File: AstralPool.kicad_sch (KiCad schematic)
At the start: 21 parts, among them J1 RJ12, J2 RJ12, J3 Header, Q1 2N3904, U1 LM2678T-5.0/NOPB

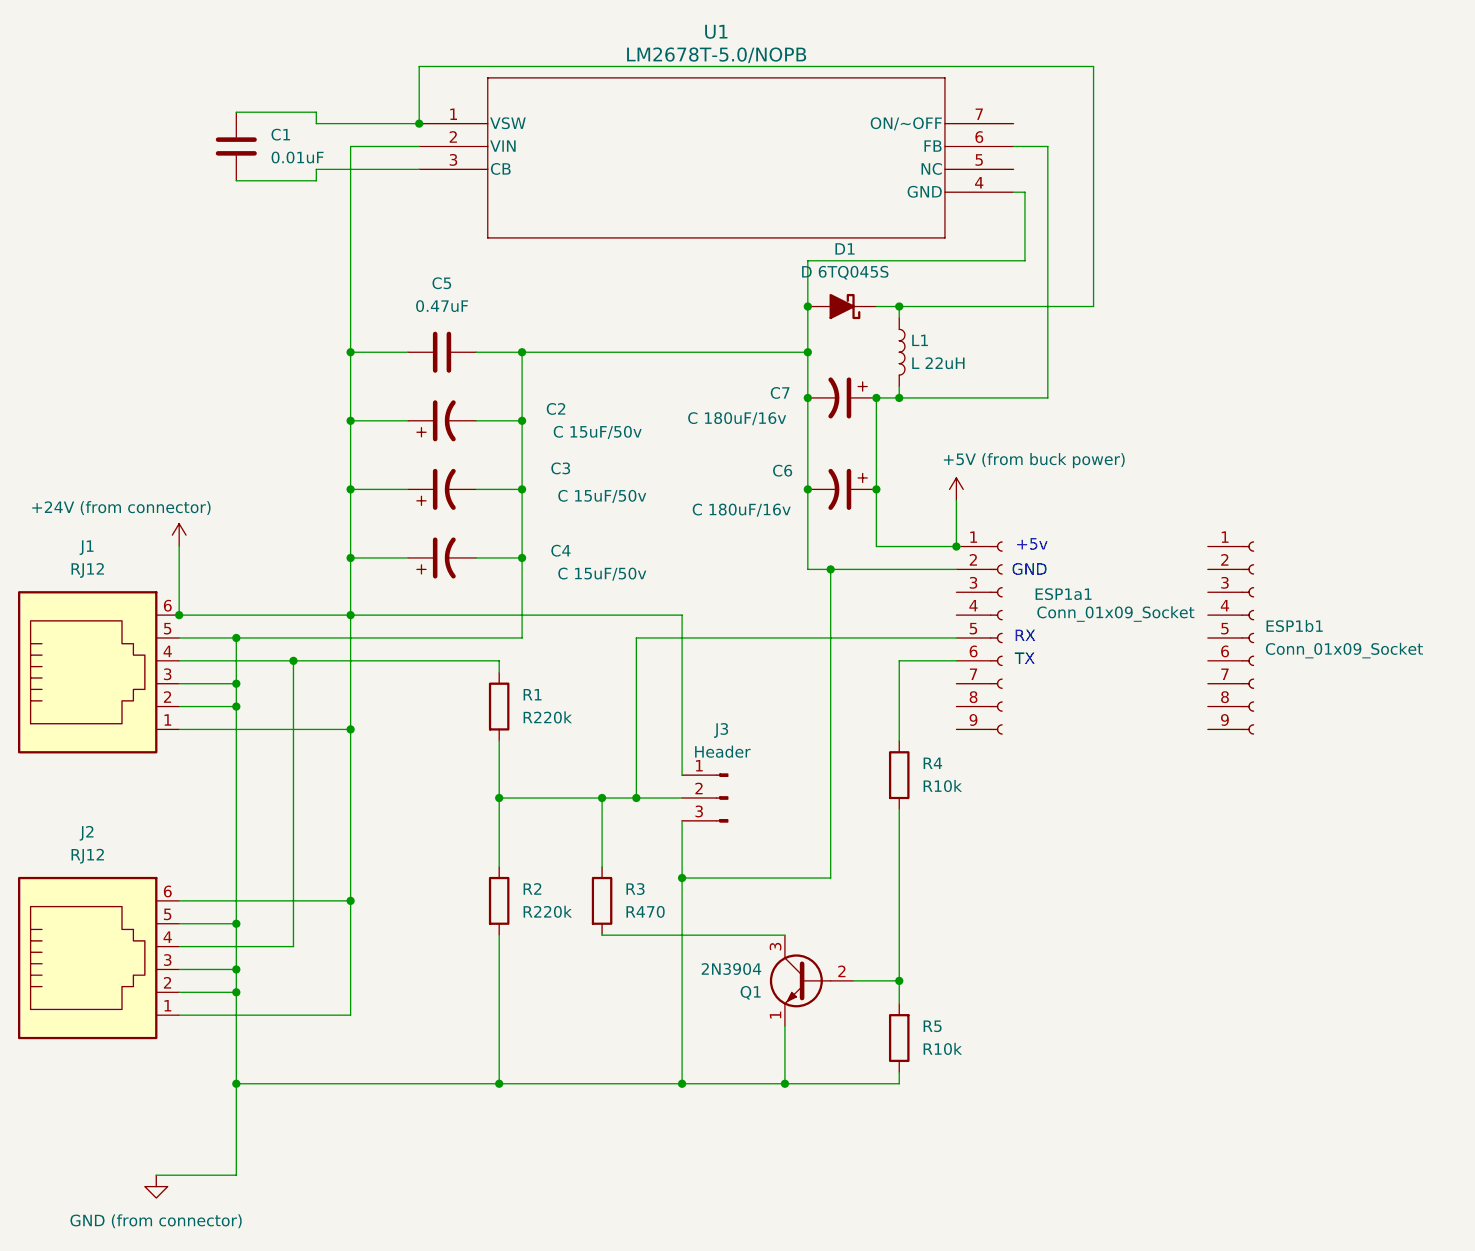
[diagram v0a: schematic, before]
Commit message: - Cleaned up all but three of the ERC failures
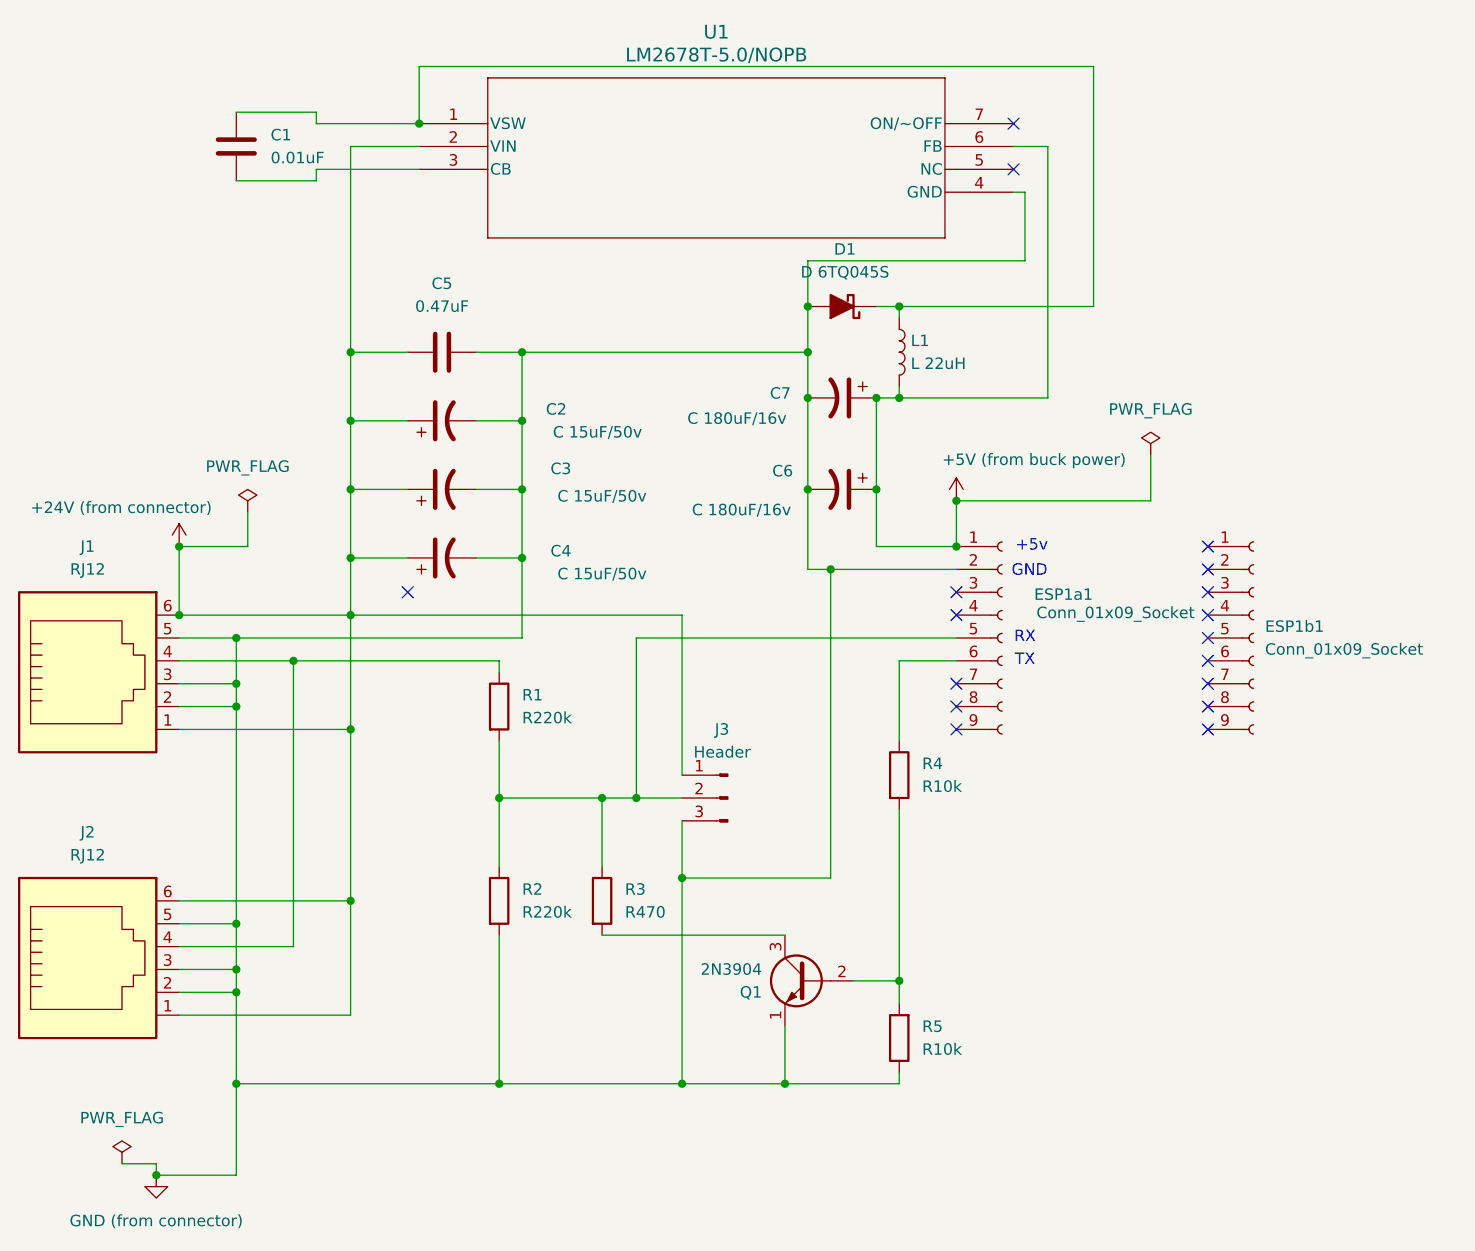
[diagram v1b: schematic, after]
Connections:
- no-connect marks 0 -> 17

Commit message: ### Fixed - Fixed all the DRC rule violations and all but one of the ERC issues - Make the component imports be relative paths
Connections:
- no-connect marks 17 -> 16
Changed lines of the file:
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@@
-	)
-	(no_connect
-		(at 83.82 88.9)
 	)
 	(no_connect

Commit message: ### Fixed - Fixed last ERC consistency issue - modified symbol needed an update
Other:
- title: (none) -> Astral Pool Controller
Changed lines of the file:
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@@
 	(generator_version "9.0")
 	(paper "A4")
+	(title_block
+		(title "Astral Pool Controller")
+		(date "2026-02-14")
+		(rev "6")
+	)
 	(text "+5v"
 		(exclude_from_sim no)
@@
 			(at 128.27 132.08 0)
 			(effects
+				(font
+					(size 1.27 1.27)
+				)
+				(hide yes)
+			)
+		)
+		(property "Sim.Device" "NPN"
+			(at 128.27 132.08 0)
+			(effects
+				(font
+					(size 1.27 1.27)
+				)
+				(hide yes)
+			)
+		)
+		(property "Sim.Pins" "1=E 2=B 3=C"
+			(at 128.27 132.08 0)
+			(effects

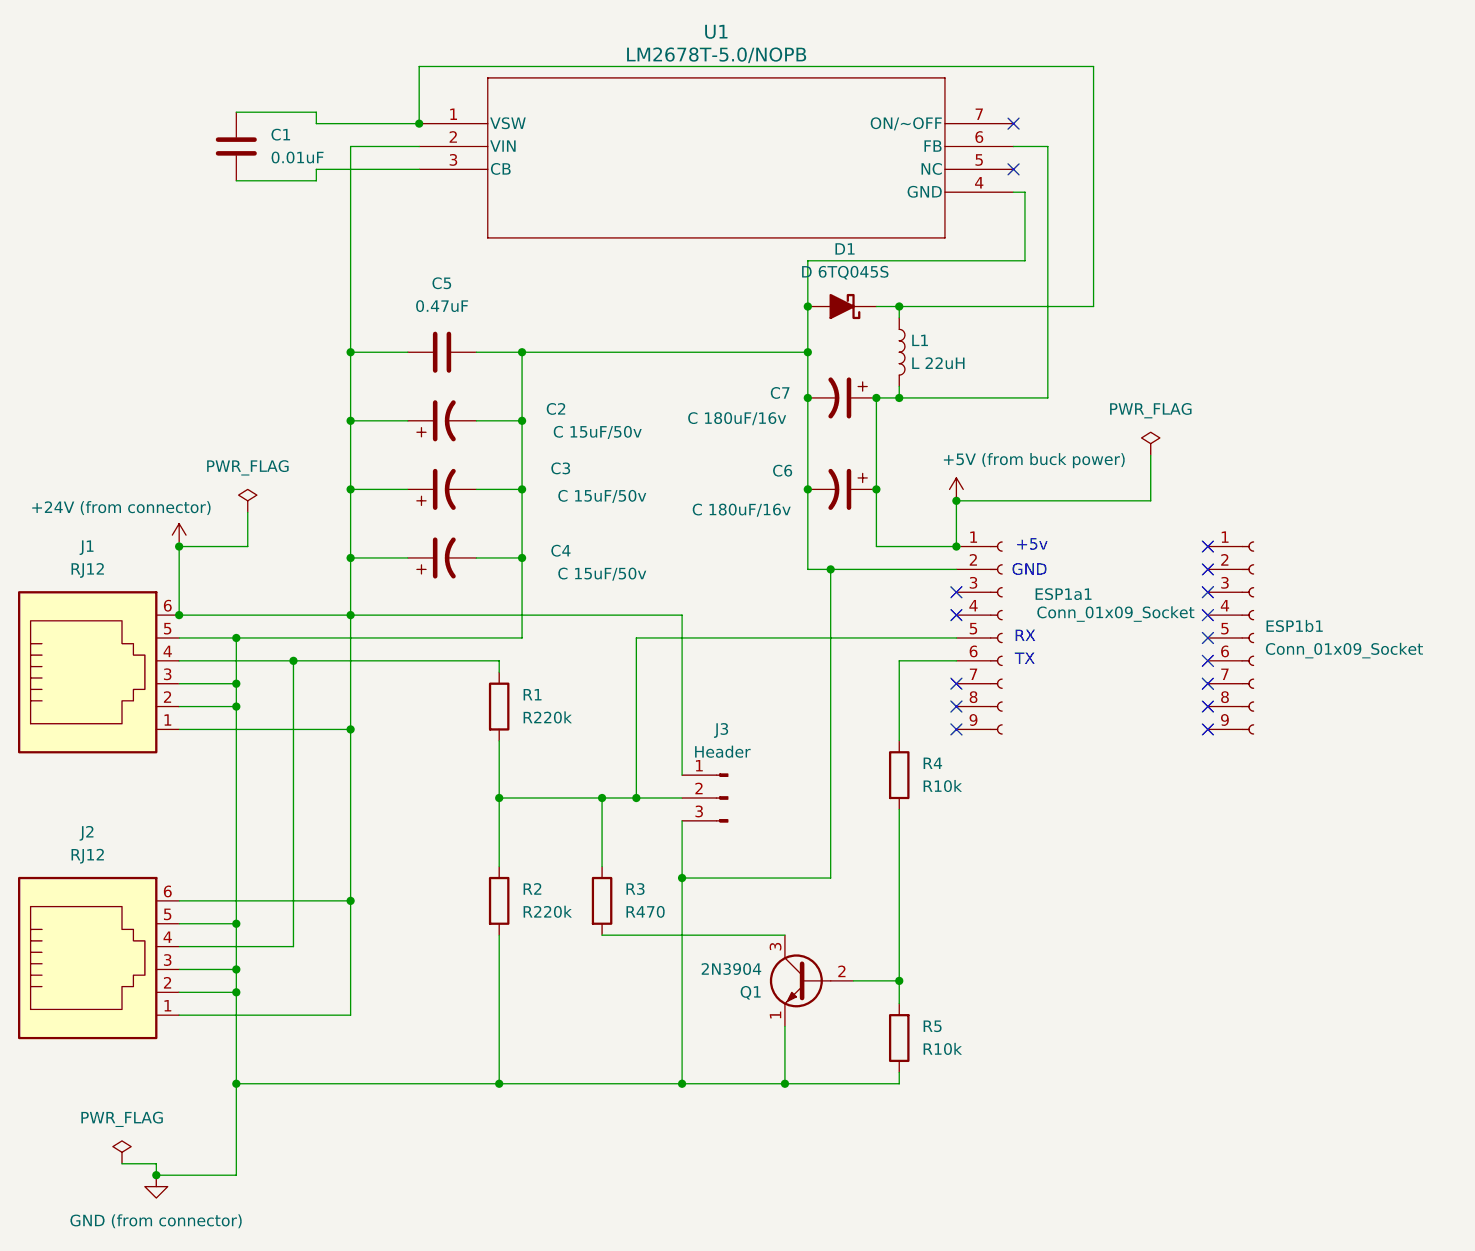
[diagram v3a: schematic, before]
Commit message: ### Added - Reworked and tested TX circuit
### Changed
- Rev 8 - Updated all footprints to correct specs
- Rev 8 - Updated components to include part numbers
- Rev 8 - Respecced the power circuit based on TI toolins
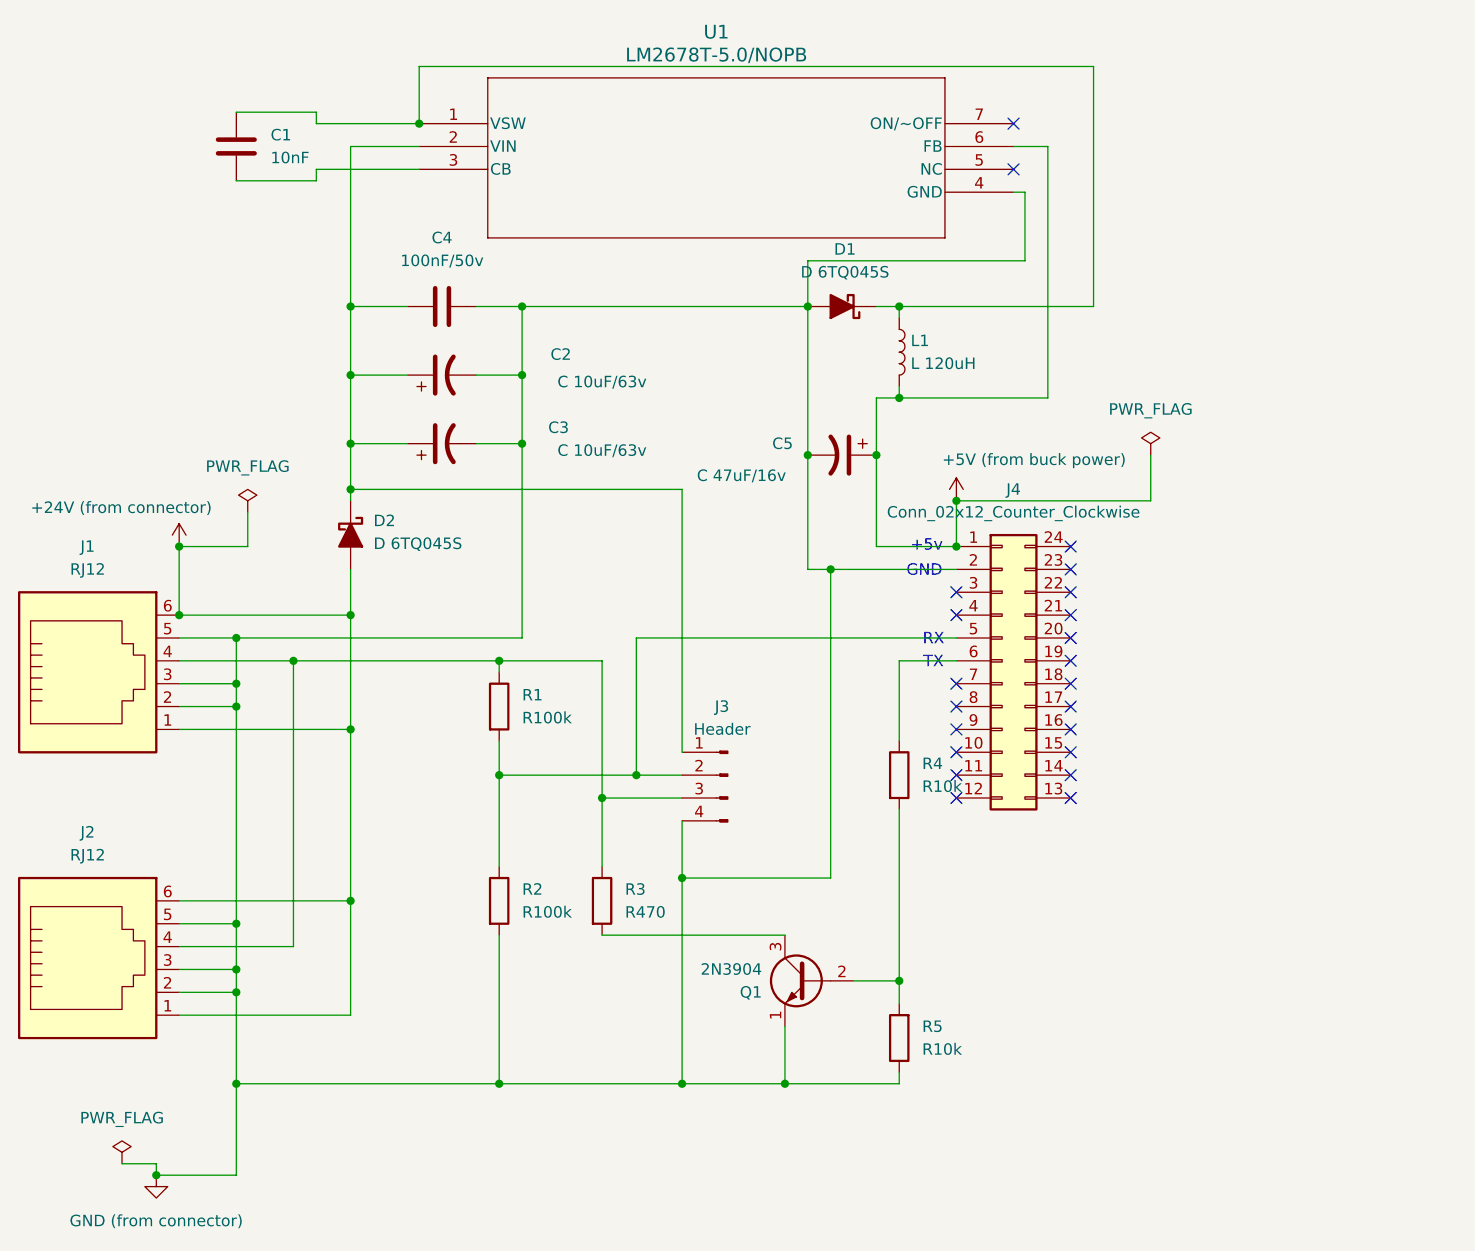
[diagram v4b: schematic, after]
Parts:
- removed C4: C 15uF/50v, Capacitor_SMD:C_1210_3225Metric, symbol Device:C_Polarized_US
- removed C7: C 180uF/16v, Capacitor_SMD:C_1210_3225Metric, symbol Device:C_Polarized_US
- removed ESP1a1, ESP1b1: Conn_01x09_Socket, Connector_PinSocket_2.54mm:PinSocket_1x09_P2.54mm_Vertical, symbol Connector:Conn_01x09_Socket
- removed J3: Header, Connector_PinHeader_2.54mm:PinHeader_1x03_P2.54mm_Vertical, symbol Connector:Conn_01x03_Pin
- added D2: D 6TQ045S, Diode_SMD:D_SOD-123F, symbol Device:D_Schottky_Filled
- added J3: Header, Connector_PinHeader_2.54mm:PinHeader_1x04_P2.54mm_Vertical, symbol Connector:Conn_01x04_Pin
- added J4: Conn_02x12_Counter_Clockwise, Package_DIP:DIP-24_18.0mmx34.29mm_W15.24mm_Socket, symbol Connector_Generic:Conn_02x12_Counter_Clockwise
- C1: value 0.01uF -> 10nF; Manufacturer (none) -> TDK; PartNum (none) -> C2012C0G1H103K060AA
- C2, C3: value C 15uF/50v -> C 10uF/63v; Manufacturer (none) -> MuRata; PartNum (none) -> GRM32ER71J106KA12L
- C4: renamed from C5; value 0.47uF -> 100nF/50v; footprint Capacitor_SMD:C_1206_3216Metric -> Capacitor_SMD:C_0805_2012Metric; Manufacturer (none) -> Kemet; PartNum (none) -> C0805C104M5RACTU
- C5: renamed from C6; value C 180uF/16v -> C 47uF/16v; Manufacturer (none) -> MuRata; PartNum (none) -> GRM32ER61C476KE15L
- D1: footprint Diode_SMD:D_2114_3652Metric -> Diode_SMD:D_SOD-123F; Manufacturer (none) -> Nexperia; PartNum (none) -> PMEG6010CEH,115
- L1: value L 22uH -> L 120uH; footprint Inductor_SMD:L_Coilcraft_LPS4414 -> Inductor_SMD:L_10.4x10.4_H4.8; Manufacturer (none) -> NIC Components; PartNum (none) -> NPI105C121MTRF
- R1, R2: value R220k -> R100k; Manufacturer (none) -> YAGEO; PartNum (none) -> RC0603FR-07100KL
- R3: Manufacturer (none) -> YAGEO; PartNum (none) -> RC0603FR-07470RL
- R4, R5: Manufacturer (none) -> YAGEO; PartNum (none) -> RC0603FR-0710KL
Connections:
- net +24V (from connector): now also D2.2 (A); no longer C2.1, C3.1, C4.1, U1.2 (VIN)
- net +5V (from buck power): now also J4.1 (Pin_1)
- net GND (from connector): now also J3.4 (Pin_4), J4.2 (Pin_2)
- net at R1.2, R2.1: now also J3.2 (Pin_2), J4.5 (Pin_5); no longer R3.1
- net at R4.1: now also J4.6 (Pin_6)
- net at J1.4, J2.4, R1.1: now also R3.1, J3.3 (Pin_3)
- new net: C2.1, C3.1, C4.1, D2.1 (K), J3.1 (Pin_1), U1.2 (VIN)
- no-connect marks 16 -> 22
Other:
- title: Astral Pool Controller -> Connect 10 Controller
- moved on the sheet: C3, C4, C5

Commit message: ### Changed - Rev 9 - Moved the power buck to surface mount component LM2678S-5.0/NOPB - Rev 9 - Moved the transistor to a SMD - Rev 9 - Added copper pour for GND on both sides - Rev 9 - Tided up annotations
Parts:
- Q1: value 2N3904 -> MMBT3904; footprint Package_TO_SOT_THT:TO-92_Inline -> Package_TO_SOT_SMD:SOT-23
- U1: value LM2678T-5.0/NOPB -> LM2678S-5.0/NOPB; footprint TA07B:TA07B -> Package_TO_SOT_SMD:TO-263-7_TabPin4; Manufacturer (none) -> Texas Instruments; PartNum (none) -> LM2678S-5.0/NOPB
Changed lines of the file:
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@@
 			)
 		)
-		(property "Value" "2N3904"
+		(property "Value" "MMBT3904"
 			(at 123.19 130.8101 0)
 			(effects
@@
 			)
 		)
-		(property "Footprint" "Package_TO_SOT_THT:TO-92_Inline"
+		(property "Footprint" "Package_TO_SOT_SMD:SOT-23"
 			(at 123.19 133.985 0)
 			(effects
@@
 			)
 		)
-		(property "Datasheet" "https://www.onsemi.com/pub/Collateral/2N3903-D.PDF"
+		(property "Datasheet" ""
 			(at 128.27 132.08 0)
 			(effects
@@
 			)
 		)
-		(property "Description" "0.2A Ic, 40V Vce, Small Signal NPN Transistor, TO-92"
+		(property "Description" ""
 			(at 128.27 132.08 0)
 			(effects
@@
 			)
 		)
-		(property "Sim.Device" "NPN"
+		(property "Sim.Device" ""
 			(at 128.27 132.08 0)
 			(effects
@@
 			)
 		)
-		(property "Sim.Pins" "1=E 2=B 3=C"
+		(property "Sim.Pins" ""
 			(at 128.27 132.08 0)
 			(effects
@@
 			)
 		)
-		(property "Value" "LM2678T-5.0/NOPB"
+		(property "Value" "LM2678S-5.0/NOPB"
 			(at 118.11 29.21 0)
 			(effects
@@
 			)
 		)
-		(property "Footprint" "TA07B:TA07B"
+		(property "Footprint" "Package_TO_SOT_SMD:TO-263-7_TabPin4"
 			(at 85.09 36.83 0)
 			(effects
@@
 			(at 85.09 36.83 0)
 			(effects
+				(font
+					(size 1.27 1.27)
+				)
+				(hide yes)
+			)
+		)
+		(property "PartNum" "LM2678S-5.0/NOPB"
+			(at 85.09 36.83 0)
+			(effects
+				(font
+					(size 1.27 1.27)
+				)
+				(hide yes)
+			)
+		)
+		(property "Manufacturer" "Texas Instruments"
+			(at 85.09 36.83 0)
+			(effects
